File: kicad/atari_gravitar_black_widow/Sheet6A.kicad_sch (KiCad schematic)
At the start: 16 parts

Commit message: Fri Night
various reviews
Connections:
- net ~{ENORM}: now also E_7.12, E_7.5, E_7.9; no longer E_7.1, E_7.1, E_7.2
- net ~{LATCH0}: now also F_7.13; no longer F_7.1
- net ~{LATCH1}: now also E_7.4; no longer E_7.1
- net ~{LATCH2}: now also E_7.13, F_7.11; no longer E_7.2, F_7.1
- net ~{LATCH3}: now also E_7.10, F_7.9; no longer E_7.2, F_7.1
- net at F_8.9 (S0), J_8.9 (S0): now also F_7.12; no longer F_7.2
- net at H_8.10 (S1): now also E_7.6; no longer E_7.3
- net at A_8.10 (S1), C_8.10 (S1): now also E_7.11; no longer E_7.3
- net at A_8.9 (S0), C_8.9 (S0): now also F_7.10; no longer F_7.2
- net at B_8.10 (S1): now also E_7.8; no longer E_7.3
- net at B_8.9 (S0): now also F_7.8; no longer F_7.2
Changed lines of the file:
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@@
     (pin "1")
   )
-  (symbol (lib_id "atari_grav_bw:LS14") (at 186.055 68.58 0) (unit 1)
+  (symbol (lib_id "atari_grav_bw:LS14") (at 186.055 68.58 0) (unit 6)
     (in_bom yes) (on_board yes)
     (property "Reference" "F_7" (id 0) (at 179.705 71.755 0))
@@
       (effects (font (size 1.27 1.27)) hide)
     )
-    (pin "14")
-    (pin "7")
-    (pin "1")
-    (pin "2")
+    (pin "12")
+    (pin "13")
   )
   (symbol (lib_id "power:GND") (at 234.315 248.92 270) (unit 1)
@@
     (pin "1")
   )
-  (symbol (lib_id "atari_grav_bw:LS00") (at 194.31 157.48 0) (mirror x) (unit 1) (convert 2)
+  (symbol (lib_id "atari_grav_bw:LS00") (at 194.31 157.48 0) (mirror x) (unit 2) (convert 2)
     (in_bom yes) (on_board yes)
     (property "Reference" "E_7" (id 0) (at 194.31 156.845 0))
@@
       (effects (font (size 1.27 1.27)) hide)
     )
-    (pin "14")
-    (pin "7")
-    (pin "1")
-    (pin "2")
-    (pin "3")
+    (pin "4")
+    (pin "5")
+    (pin "6")
   )
   (symbol (lib_id "atari_grav_bw:LS14") (at 186.055 167.64 0) (unit 1)
@@
     (pin "1")
   )
-  (symbol (lib_id "atari_grav_bw:LS00") (at 194.31 208.28 0) (unit 1) (convert 2)
+  (symbol (lib_id "atari_grav_bw:LS00") (at 194.31 208.28 0) (unit 4) (convert 2)
     (in_bom yes) (on_board yes)
     (property "Reference" "E_7" (id 0) (at 194.31 209.55 0))
@@
       (effects (font (size 1.27 1.27)) hide)
     )
-    (pin "14")
-    (pin "7")
-    (pin "1")
-    (pin "2")
-    (pin "3")
-  )
-  (symbol (lib_id "atari_grav_bw:LS14") (at 186.055 218.44 0) (unit 1)
+    (pin "11")
+    (pin "12")
+    (pin "13")
+  )
+  (symbol (lib_id "atari_grav_bw:LS14") (at 186.055 218.44 0) (unit 5)
     (in_bom yes) (on_board yes)
     (property "Reference" "F_7" (id 0) (at 179.07 220.345 0))
@@
       (effects (font (size 1.27 1.27)) hide)
     )
-    (pin "14")
-    (pin "7")
-    (pin "1")
-    (pin "2")
-  )
-  (symbol (lib_id "atari_grav_bw:LS14") (at 185.42 317.5 0) (unit 1)
+    (pin "10")
+    (pin "11")
+  )
+  (symbol (lib_id "atari_grav_bw:LS14") (at 185.42 317.5 0) (unit 4)
     (in_bom yes) (on_board yes)
     (property "Reference" "F_7" (id 0) (at 178.435 319.405 0))
@@
       (effects (font (size 1.27 1.27)) hide)
     )
-    (pin "14")
-    (pin "7")
-    (pin "1")
-    (pin "2")
-  )
-  (symbol (lib_id "atari_grav_bw:LS00") (at 193.675 307.34 0) (unit 1) (convert 2)
+    (pin "8")
+    (pin "9")
+  )
+  (symbol (lib_id "atari_grav_bw:LS00") (at 193.675 307.34 0) (unit 3) (convert 2)
     (in_bom yes) (on_board yes)
     (property "Reference" "E_7" (id 0) (at 193.675 306.07 0))
@@
       (effects (font (size 1.27 1.27)) hide)
     )
-    (pin "14")
-    (pin "7")
-    (pin "1")
-    (pin "2")
-    (pin "3")
+    (pin "10")
+    (pin "8")
+    (pin "9")
   )
   (symbol (lib_id "power:+5V") (at 409.575 172.085 0) (unit 1)

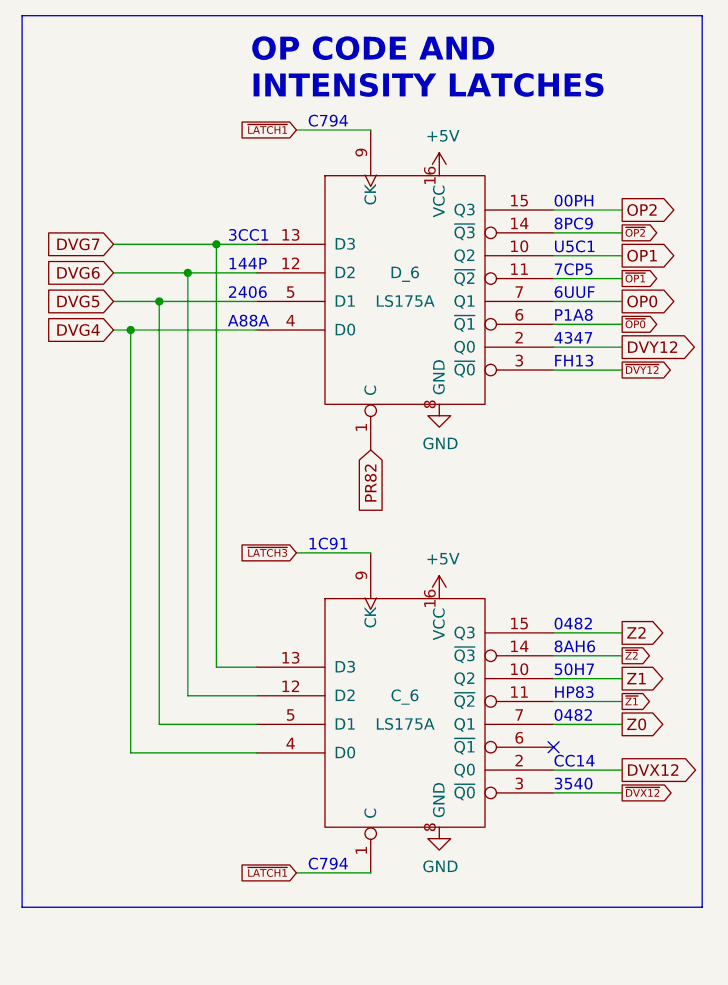
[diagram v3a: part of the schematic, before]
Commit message: Fixed all warnings and errors
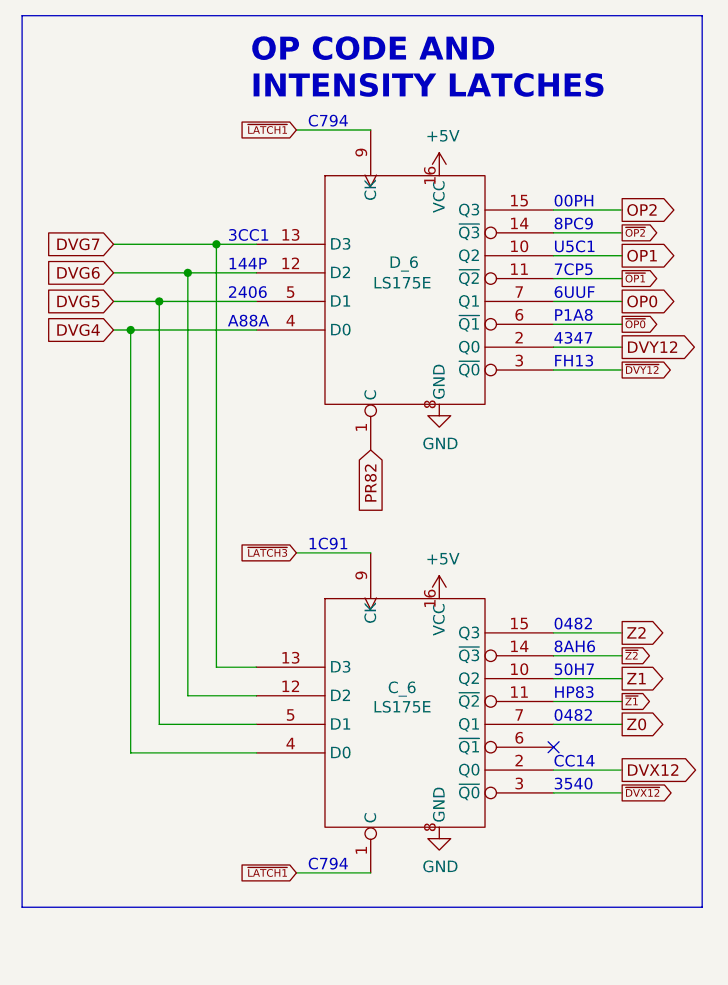
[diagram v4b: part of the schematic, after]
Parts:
- removed C_6, D_6: LS175A, symbol atari_grav_bw:LS175A
- added C_6, D_6: LS175E, symbol atari_grav_bw:LS175E
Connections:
- net +5V: now also C_6.16 (VCC), D_6.16 (VCC)
- net DVG4: now also C_6.4 (D0), D_6.4 (D0)
- net DVG5: now also C_6.5 (D1), D_6.5 (D1)
- net DVG6: now also C_6.12 (D2), D_6.12 (D2)
- net DVG7: now also C_6.13 (D3), D_6.13 (D3)
- net DVX12: now also C_6.2 (Q0)
- net DVY12: now also D_6.2 (Q0)
- net GND: now also C_6.8 (GND), D_6.8 (GND)
- net OP0: now also D_6.7 (Q1)
- net OP1: now also D_6.10 (Q2)
- net OP2: now also D_6.15 (Q3)
- net PR82: now also D_6.1 (C)
- net Z0: now also C_6.7 (Q1)
- net Z1: now also C_6.10 (Q2)
- net Z2: now also C_6.15 (Q3)
- net ~{DVX12}: now also C_6.3 (~{Q0})
- net ~{DVY12}: now also D_6.3 (~{Q0})
- net ~{LATCH1}: now also C_6.1 (C), D_6.9 (CK)
- net ~{LATCH3}: now also C_6.9 (CK)
- net ~{OP0}: now also D_6.6 (~{Q1})
- net ~{OP1}: now also D_6.11 (~{Q2})
- net ~{OP2}: now also D_6.14 (~{Q3})
- net ~{Z1}: now also C_6.11 (~{Q2})
- net ~{Z2}: now also C_6.14 (~{Q3})
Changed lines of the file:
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@@
     (pin "1")
   )
-  (symbol (lib_id "atari_grav_bw:LS175A") (at 405.765 184.785 0) (unit 1)
+  (symbol (lib_id "atari_grav_bw:LS175E") (at 405.765 185.42 0) (unit 1)
     (in_bom yes) (on_board yes)
-    (property "Reference" "D_6" (id 0) (at 405.765 182.88 0))
-    (property "Value" "LS175A" (id 1) (at 405.765 186.055 0))
-    (property "Footprint" "" (id 2) (at 405.765 184.785 0)
+    (property "Reference" "D_6" (id 0) (at 403.987 181.737 0)
+      (effects (font (size 1.27 1.27)) (justify left))
+    )
+    (property "Value" "LS175E" (id 1) (at 402.209 184.023 0)
+      (effects (font (size 1.27 1.27)) (justify left))
+    )
+    (property "Footprint" "" (id 2) (at 405.765 185.42 0)
       (effects (font (size 1.27 1.27)) hide)
     )
-    (property "Datasheet" "" (id 3) (at 405.765 184.785 0)
+    (property "Datasheet" "" (id 3) (at 405.765 185.42 0)
       (effects (font (size 1.27 1.27)) hide)
     )
@@
     (pin "9")
   )
-  (symbol (lib_id "atari_grav_bw:LS175A") (at 405.765 231.775 0) (unit 1)
+  (symbol (lib_id "atari_grav_bw:LS175E") (at 405.765 232.41 0) (unit 1)
     (in_bom yes) (on_board yes)
-    (property "Reference" "C_6" (id 0) (at 405.765 229.87 0))
-    (property "Value" "LS175A" (id 1) (at 405.765 233.045 0))
-    (property "Footprint" "" (id 2) (at 405.765 231.775 0)
+    (property "Reference" "C_6" (id 0) (at 403.86 228.981 0)
+      (effects (font (size 1.27 1.27)) (justify left))
+    )
+    (property "Value" "LS175E" (id 1) (at 402.209 231.14 0)
+      (effects (font (size 1.27 1.27)) (justify left))
+    )
+    (property "Footprint" "" (id 2) (at 405.765 232.41 0)
       (effects (font (size 1.27 1.27)) hide)
     )
-    (property "Datasheet" "" (id 3) (at 405.765 231.775 0)
+    (property "Datasheet" "" (id 3) (at 405.765 232.41 0)
       (effects (font (size 1.27 1.27)) hide)
     )

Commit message: place ttl
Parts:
- A_8, B_8: footprint (none) -> Star_Wars_Vector_PCB:DIP16
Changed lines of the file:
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@@
       (effects (font (size 1.27 1.27)) (justify left))
     )
-    (property "Footprint" "" (id 2) (at 236.855 237.49 0)
+    (property "Footprint" "Star_Wars_Vector_PCB:DIP16" (id 2) (at 236.855 237.49 0)
       (effects (font (size 1.27 1.27)) hide)
     )
@@
       (effects (font (size 1.27 1.27)) (justify left))
     )
-    (property "Footprint" "" (id 2) (at 236.855 336.55 0)
+    (property "Footprint" "Star_Wars_Vector_PCB:DIP16" (id 2) (at 236.855 336.55 0)
       (effects (font (size 1.27 1.27)) hide)
     )

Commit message: more ttl placements
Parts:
- C_6, C_8, D_6, F_8, H_8: footprint (none) -> Star_Wars_Vector_PCB:DIP16
- E_7, F_7: footprint (none) -> Star_Wars_Vector_PCB:DIP14
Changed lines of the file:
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@@
       (effects (font (size 1.27 1.27)) (justify left))
     )
-    (property "Footprint" "" (id 2) (at 236.855 87.63 0)
+    (property "Footprint" "Star_Wars_Vector_PCB:DIP16" (id 2) (at 236.855 87.63 0)
       (effects (font (size 1.27 1.27)) hide)
     )
@@
       (effects (font (size 1.27 1.27)) (justify left))
     )
-    (property "Footprint" "" (id 2) (at 236.855 186.69 0)
+    (property "Footprint" "Star_Wars_Vector_PCB:DIP16" (id 2) (at 236.855 186.69 0)
       (effects (font (size 1.27 1.27)) hide)
     )
@@
       (effects (font (size 1.27 1.27)) (justify left))
     )
-    (property "Footprint" "" (id 2) (at 194.945 58.42 0)
+    (property "Footprint" "Star_Wars_Vector_PCB:DIP14" (id 2) (at 194.945 58.42 0)
       (effects (font (size 1.27 1.27)) hide)
     )
@@
     (property "Reference" "F_7" (id 0) (at 179.705 71.755 0))
     (property "Value" "LS14" (id 1) (at 179.705 69.85 0))
-    (property "Footprint" "" (id 2) (at 188.595 68.58 0)
+    (property "Footprint" "Star_Wars_Vector_PCB:DIP14" (id 2) (at 188.595 68.58 0)
       (effects (font (size 1.27 1.27)) hide)
     )
@@
       (effects (font (size 1.27 1.27)) (justify left))
     )
-    (property "Footprint" "" (id 2) (at 236.855 286.385 0)
+    (property "Footprint" "Star_Wars_Vector_PCB:DIP16" (id 2) (at 236.855 286.385 0)
       (effects (font (size 1.27 1.27)) hide)
     )
@@
     (property "Reference" "E_7" (id 0) (at 194.31 156.845 0))
     (property "Value" "S00" (id 1) (at 194.31 158.75 0))
-    (property "Footprint" "" (id 2) (at 194.31 157.48 0)
+    (property "Footprint" "Star_Wars_Vector_PCB:DIP14" (id 2) (at 194.31 157.48 0)
       (effects (font (size 1.27 1.27)) hide)
     )
@@
     (property "Reference" "F_7" (id 0) (at 179.705 168.91 0))
     (property "Value" "LS14" (id 1) (at 194.31 168.91 0))
-    (property "Footprint" "" (id 2) (at 188.595 167.64 0)
+    (property "Footprint" "Star_Wars_Vector_PCB:DIP14" (id 2) (at 188.595 167.64 0)
       (effects (font (size 1.27 1.27)) hide)
     )
@@
     (property "Reference" "E_7" (id 0) (at 194.31 209.55 0))
     (property "Value" "S00" (id 1) (at 194.31 207.645 0))
-    (property "Footprint" "" (id 2) (at 194.31 208.28 0)
+    (property "Footprint" "Star_Wars_Vector_PCB:DIP14" (id 2) (at 194.31 208.28 0)
       (effects (font (size 1.27 1.27)) hide)
     )
@@
     (property "Reference" "F_7" (id 0) (at 179.07 220.345 0))
     (property "Value" "LS14" (id 1) (at 191.135 220.345 0))
-    (property "Footprint" "" (id 2) (at 188.595 218.44 0)
+    (property "Footprint" "Star_Wars_Vector_PCB:DIP14" (id 2) (at 188.595 218.44 0)
       (effects (font (size 1.27 1.27)) hide)
     )
@@
     (property "Reference" "F_7" (id 0) (at 178.435 319.405 0))
     (property "Value" "LS14" (id 1) (at 189.865 319.405 0))
-    (property "Footprint" "" (id 2) (at 187.96 317.5 0)
+    (property "Footprint" "Star_Wars_Vector_PCB:DIP14" (id 2) (at 187.96 317.5 0)
       (effects (font (size 1.27 1.27)) hide)
     )
@@
     (property "Reference" "E_7" (id 0) (at 193.675 306.07 0))
     (property "Value" "S00" (id 1) (at 193.675 308.61 0))
-    (property "Footprint" "" (id 2) (at 193.675 307.34 0)
+    (property "Footprint" "Star_Wars_Vector_PCB:DIP14" (id 2) (at 193.675 307.34 0)
       (effects (font (size 1.27 1.27)) hide)
     )
@@
       (effects (font (size 1.27 1.27)) (justify left))
     )
-    (property "Footprint" "" (id 2) (at 405.765 185.42 0)
+    (property "Footprint" "Star_Wars_Vector_PCB:DIP16" (id 2) (at 405.765 185.42 0)
       (effects (font (size 1.27 1.27)) hide)
     )
@@
       (effects (font (size 1.27 1.27)) (justify left))
     )
-    (property "Footprint" "" (id 2) (at 405.765 232.41 0)
-      (effects (font (size 1.27 1.27)) hide)
-    )
+    (property "Footprint" "Star_Wars_Vector_PCB:DIP16" (id 2) (at 405.765 232.41 0)
+      (effects (font (size 1.27 1.27)) hide)
+    )

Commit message: more chip layouts
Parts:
- J_8: footprint (none) -> Star_Wars_Vector_PCB:DIP16
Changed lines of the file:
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@@
       (effects (font (size 1.27 1.27)) (justify left))
     )
-    (property "Footprint" "" (id 2) (at 236.855 135.89 0)
+    (property "Footprint" "Star_Wars_Vector_PCB:DIP16" (id 2) (at 236.855 135.89 0)
       (effects (font (size 1.27 1.27)) hide)
     )

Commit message: lots o' traces
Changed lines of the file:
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@@
     (pin "1")
   )
-  (symbol (lib_id "atari_grav_bw:LS00") (at 194.31 157.48 0) (mirror x) (unit 2) (convert 2)
+  (symbol (lib_name "LS00_1") (lib_id "atari_grav_bw:LS00") (at 194.31 157.48 0) (mirror x) (unit 2) (convert 2)
     (in_bom yes) (on_board yes)
-    (property "Reference" "E_7" (id 0) (at 194.31 156.845 0))
-    (property "Value" "S00" (id 1) (at 194.31 158.75 0))
+    (property "Reference" "E_7" (id 0) (at 194.31 158.115 0))
+    (property "Value" "S00" (id 1) (at 194.31 156.21 0))
     (property "Footprint" "Star_Wars_Vector_PCB:DIP14" (id 2) (at 194.31 157.48 0)
       (effects (font (size 1.27 1.27)) hide)
